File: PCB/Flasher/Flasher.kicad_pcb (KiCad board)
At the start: 2 copper layers, 70 x 70 mm, 60 parts, among them J1 Reset, J2 RJ12, J3 USB, J4 USB-C-Socket-V, J5 TF_PUSH, SW1 SW_Push_DPDT, U1 ESP32-S3-MINI-1, U2 TPS562246, U3 FT231XQ, U4 TPS22916CNYFPR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

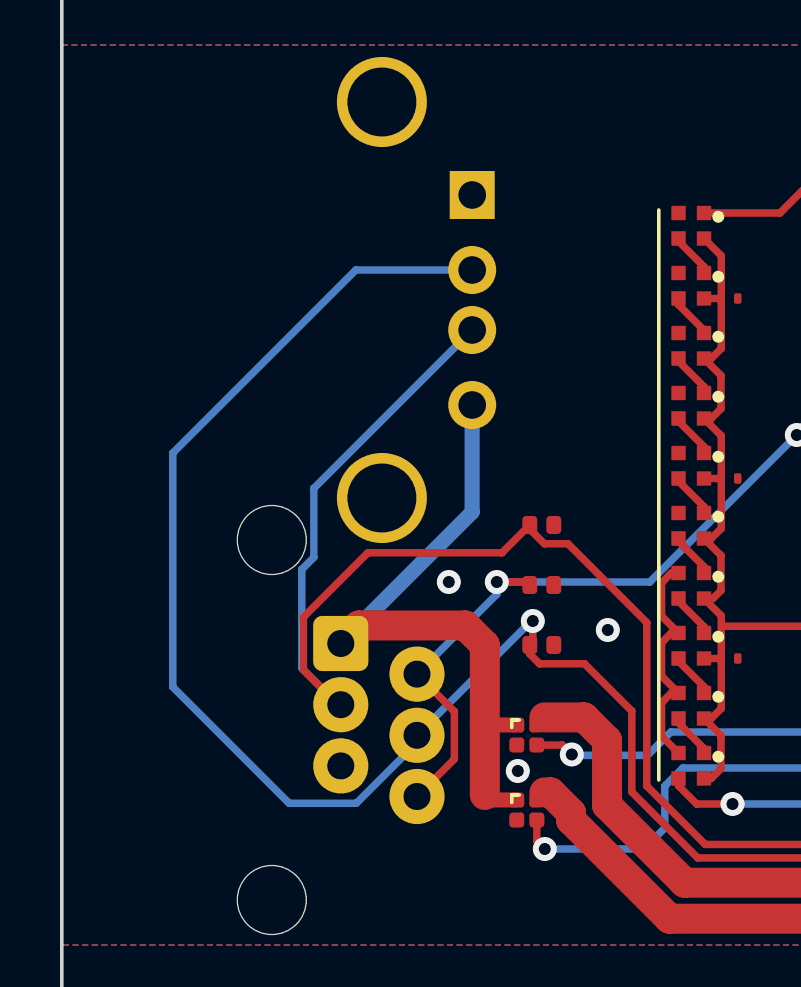
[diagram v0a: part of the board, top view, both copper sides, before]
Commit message: Reverse USB, FFS
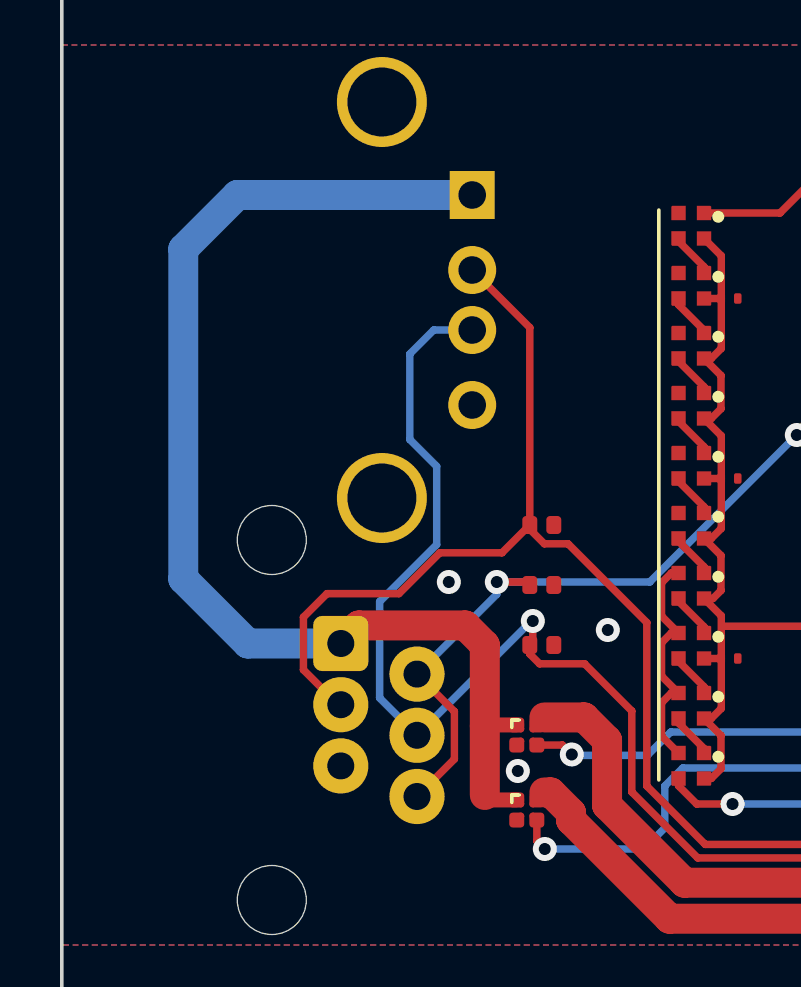
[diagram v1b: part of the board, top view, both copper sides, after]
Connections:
- J3 pad 1: GND -> VOUT
- J3 pad 2: D+ -> D-
- J3 pad 3: D- -> D+
- J3 pad 4: VOUT -> GND
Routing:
- net VOUT: track 22.3 -> 40.0 mm
- net D+: track 81.3 -> 67.2 mm
- net D-: track 73.8 -> 67.7 mm

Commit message: PCB update
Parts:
- added C17: 220uF Tant, RevK:CP_EIA-3528-21_Kemet-B, F.Cu at (138.0, 73.5)
- added C35: 220uF Tant, RevK:CP_EIA-3528-21_Kemet-B, F.Cu at (142.0, 73.5)
- moved D13 10.5 mm to (116.0, 59.5)
- moved D12 8.50 mm to (116.0, 57.5)
- moved C7 1.50 mm to (157.0, 77.5)
- moved C1 1.12 mm to (157.0, 73.5), turned to -90 degrees
- moved R4 0.87 mm to (160.6, 71.6), turned to 180 degrees
- moved C3 0.50 mm to (159.8, 72.7)
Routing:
- net D-: track 67.7 -> 76.7 mm, vias 0 -> 2
- net VBUS: track 78.2 -> 82.3 mm
- net D+: track 67.2 -> 69.7 mm
- net +3.3V: track 181.6 -> 182.3 mm
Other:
- board text added: "0%"
- board text added: "100%"

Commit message: LED update
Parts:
- D1, D10, D11, D2, D3, D4, D5, D6, D7, D8, D9: footprint RevK:SMD1010 -> RevK:SMD1615
- moved R8 4.78 mm to (161.0, 59.8), turned to 0 degrees
- moved C14 1.19 mm to (122.7, 59.5)
- moved C15 1.19 mm to (122.7, 65.5)
- moved C16 1.19 mm to (122.7, 71.5)
- moved D11 0.25 mm to (126.7, 51.5)
- turned D1 to 0 degrees
- turned D10 to 0 degrees
- turned D2 to 0 degrees
- turned D3 to 0 degrees
- turned D4 to 0 degrees
- turned D5 to 0 degrees
- turned D6 to 0 degrees
- turned D7 to 0 degrees
- turned D8 to 0 degrees
- turned D9 to 0 degrees
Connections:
- D1 pad 1: Net-(D1-O) -> GND
- D1 pad 2: +3.3V -> LED
- D1 pad 3: GND -> +3.3V
- D1 pad 4: LED -> Net-(D1-I)
- D10 pad 1: Net-(D10-O) -> GND
- D10 pad 2: +3.3V -> Net-(D10-+)
- D10 pad 3: GND -> +3.3V
- D11 pad 1: unconnected-(D11-O-Pad1) -> GND
- D11 pad 2: +3.3V -> Net-(D10-I)
- D11 pad 3: GND -> +3.3V
- D11 pad 4: Net-(D10-O) -> Net-(D11-O)
- D2 pad 1: Net-(D2-O) -> GND
- D2 pad 2: +3.3V -> Net-(D1-I)
- D2 pad 3: GND -> +3.3V
- D2 pad 4: Net-(D1-O) -> Net-(D2-I)
- D3 pad 1: Net-(D3-O) -> GND
- D3 pad 2: +3.3V -> Net-(D2-I)
- D3 pad 3: GND -> +3.3V
- D3 pad 4: Net-(D2-O) -> Net-(D3-I)
- D4 pad 1: Net-(D4-O) -> GND
- D4 pad 2: +3.3V -> Net-(D3-I)
- D4 pad 3: GND -> +3.3V
- D4 pad 4: Net-(D3-O) -> Net-(D4-I)
- D5 pad 1: Net-(D5-O) -> GND
- D5 pad 2: +3.3V -> Net-(D4-I)
- D5 pad 3: GND -> +3.3V
- D5 pad 4: Net-(D4-O) -> Net-(D5-I)
- D6 pad 1: Net-(D6-O) -> GND
- D6 pad 2: +3.3V -> Net-(D5-I)
- D6 pad 3: GND -> +3.3V
- D6 pad 4: Net-(D5-O) -> Net-(D6-I)
- D7 pad 1: Net-(D7-O) -> GND
- D7 pad 2: +3.3V -> Net-(D6-I)
- D7 pad 3: GND -> +3.3V
- D7 pad 4: Net-(D6-O) -> Net-(D7-I)
- D8 pad 1: Net-(D8-O) -> GND
- D8 pad 2: +3.3V -> Net-(D7-I)
- D8 pad 3: GND -> +3.3V
- D8 pad 4: Net-(D7-O) -> Net-(D8-I)
- D9 pad 1: Net-(D10-I) -> GND
- D9 pad 2: +3.3V -> Net-(D8-I)
- D9 pad 3: GND -> +3.3V
- D9 pad 4: Net-(D8-O) -> Net-(D10-+)
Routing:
- net Net-(D10-I): track 1.41 -> 9.57 mm
- net GND: track 35.2 -> 27.4 mm
- net Net-(D10-O): track 7.61 -> 0.00 mm
- net +3.3V: track 182.3 -> 185.9 mm
- net Net-(J4-CC2): track 5.45 -> 7.38 mm
- net Net-(D8-I): track 0.00 -> 1.68 mm
- net Net-(D7-I): track 0.00 -> 1.68 mm
- net Net-(D6-I): track 0.00 -> 1.68 mm
- net Net-(D5-I): track 0.00 -> 1.68 mm
- net Net-(D4-I): track 0.00 -> 1.68 mm
- net Net-(D3-I): track 0.00 -> 1.68 mm
- net Net-(D2-I): track 0.00 -> 1.68 mm
- net Net-(D10-+): track 0.00 -> 1.68 mm
- net Net-(D1-I): track 0.00 -> 1.68 mm
- net Net-(D1-O): track 1.50 -> 0.00 mm
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
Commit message: New LED
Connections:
- C14 pad 1: +3.3V -> VBUS
- C15 pad 1: +3.3V -> VBUS
- C16 pad 1: +3.3V -> VBUS
- D1 pad 3: +3.3V -> VBUS
- D10 pad 3: +3.3V -> VBUS
- D11 pad 3: +3.3V -> VBUS
- D11 pad 4: Net-(D11-O) -> unconnected-(D11-O-Pad4)
- D2 pad 3: +3.3V -> VBUS
- D3 pad 3: +3.3V -> VBUS
- D4 pad 3: +3.3V -> VBUS
- D5 pad 3: +3.3V -> VBUS
- D6 pad 3: +3.3V -> VBUS
- D7 pad 3: +3.3V -> VBUS
- D8 pad 3: +3.3V -> VBUS
- D9 pad 3: +3.3V -> VBUS
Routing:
- net +3.3V: track 185.9 -> 131.5 mm
- net VBUS: track 82.3 -> 123.3 mm

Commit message: Library update
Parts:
- U1: value ESP32-S3-MINI-1 -> ESP32-S3-MINI-1-N4R2
- turned SW1 to 180 degrees

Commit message: Library update
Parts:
- moved C14 2.95 mm to (122.8, 56.6)
- moved D10 2.52 mm to (121.0, 53.5)
- moved D9 2.02 mm to (121.0, 56.0)
- moved D1 1.97 mm to (121.0, 76.0)
- moved D8 1.52 mm to (121.0, 58.5)
- moved D2 1.47 mm to (121.0, 73.5)
- moved C15 1.35 mm to (122.8, 64.2)
- moved D7 1.02 mm to (121.0, 61.0)
- moved D3 0.97 mm to (121.0, 71.0)
- moved D6 0.53 mm to (121.0, 63.5)
- moved D4 0.47 mm to (121.0, 68.5)
- moved C16 0.17 mm to (122.8, 71.7)
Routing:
- net GND: track 27.4 -> 33.4 mm
- net VBUS: track 123.3 -> 125.5 mm
- net Net-(D10-O): track 9.57 -> 7.59 mm
- net +3.3V: track 131.5 -> 132.9 mm
